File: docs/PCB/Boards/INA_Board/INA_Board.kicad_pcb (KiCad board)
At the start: 2 copper layers, 64.2 x 35.6 mm, 24 parts, among them J1 COM, J2 INA, Q1 AO3407A, SW1 SW_DIP_x02, U1 INA226AIDGST, U2 SIP32431DR3-T1GE3

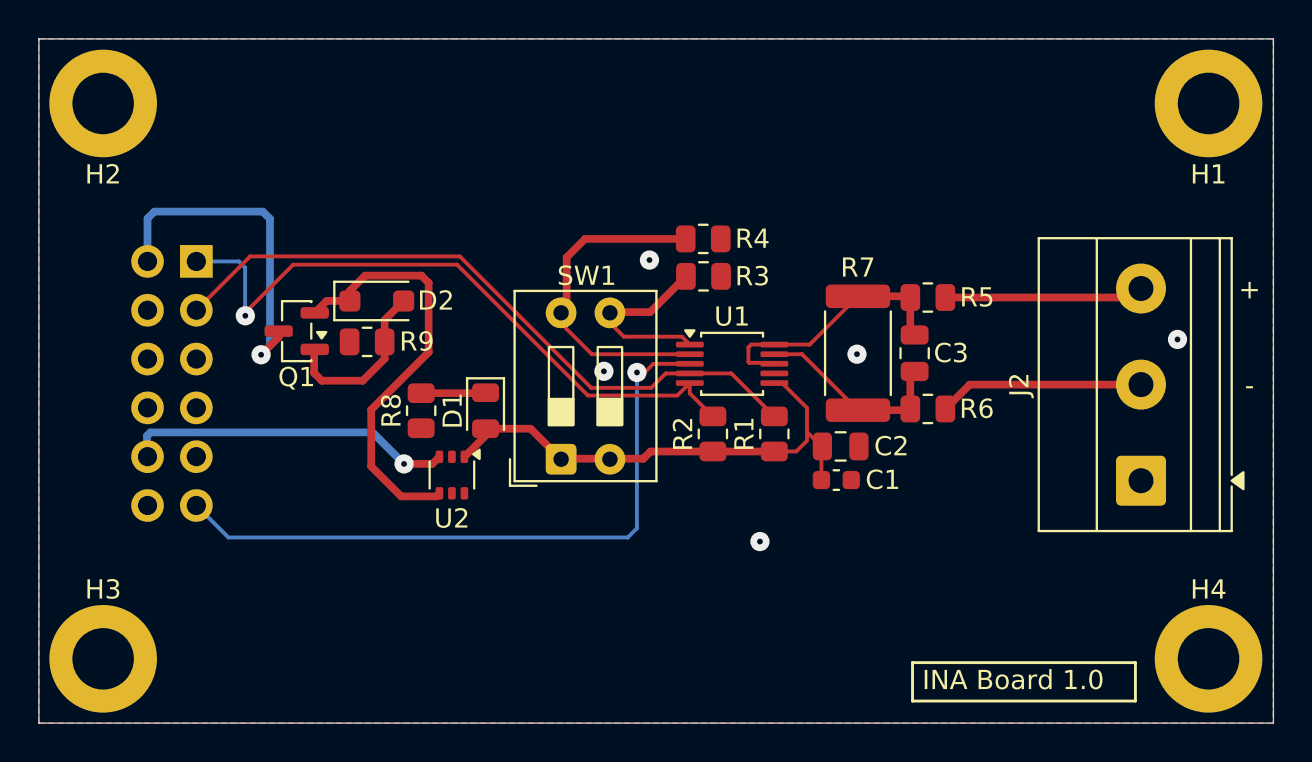
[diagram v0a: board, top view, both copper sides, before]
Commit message: Test program added, can protocol added.
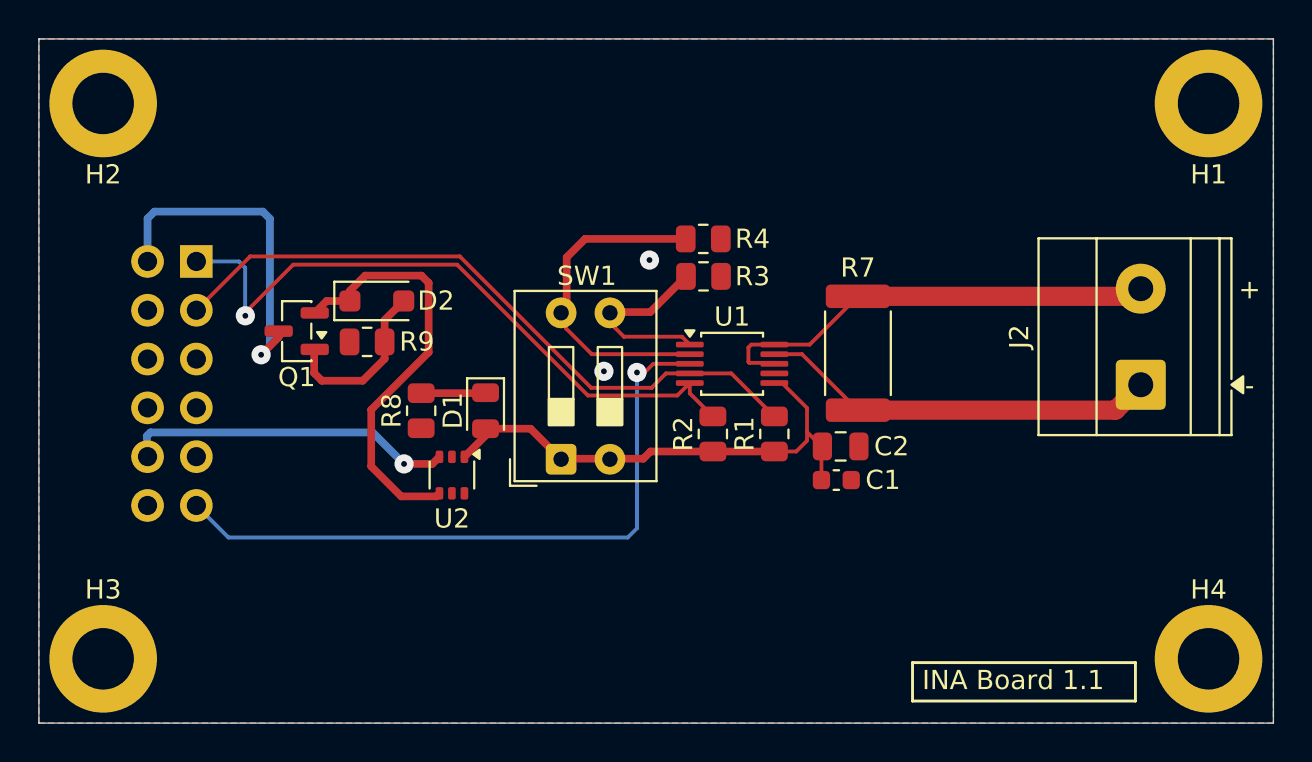
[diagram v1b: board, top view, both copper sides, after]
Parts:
- removed C3: 100nF, Capacitor_SMD:C_0805_2012Metric
- removed R5, R6: 10, Resistor_SMD:R_0805_2012Metric
- J2: footprint TerminalBlock_Phoenix:TerminalBlock_Phoenix_MKDS-1,5-3_1x03_P5.00mm_Horizontal -> TerminalBlock_Phoenix:TerminalBlock_Phoenix_MKDS-1,5-2_1x02_P5.00mm_Horizontal
- moved J2 4.99 mm to (172.9, 83.7)
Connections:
- J2 pad 1: GND -> INA-
- J2 pad 2: INA- -> INA+
- R7 pad 1: Net-(U1-Vbus) -> INA+
- R7 pad 2: Net-(U1-Vin-) -> INA-
- U1 pad 10: Net-(U1-Vbus) -> INA+
- U1 pad 8: Net-(U1-Vbus) -> INA+
- U1 pad 9: Net-(U1-Vin-) -> INA-
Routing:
- net INA+: track 10.4 -> 24.4 mm
- net Net-(U1-Vbus): track 13.5 -> 0.00 mm
- net Net-(U1-Vin-): track 10.4 -> 0.00 mm
- net INA-: track 10.7 -> 20.9 mm
- net GND: vias 5 -> 2
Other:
- board text added: "INA Board 1.1"
- board text removed: "INA Board 1.0"

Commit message: Boards modified.
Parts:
- added C3: 100nF, Capacitor_SMD:C_0805_2012Metric, F.Cu at (157.5, 81.5)
- added C4: 100nF, Capacitor_SMD:C_0805_2012Metric, F.Cu at (155.6, 73.8)
- added R10: 10R, Resistor_SMD:R_0805_2012Metric, F.Cu at (155.6, 75.8)
- added R5: 10R, Resistor_SMD:R_0805_2012Metric, F.Cu at (160.5, 78.7)
- added R6: 10R, Resistor_SMD:R_0805_2012Metric, F.Cu at (160.6, 84.7)
- moved R7 6.64 mm to (164.8, 81.5)
- moved U1 0.99 mm to (152.7, 82.6)
- moved C1 0.69 mm to (157.1, 89.3)
- moved C2 0.69 mm to (157.3, 87.6)
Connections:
- U1 pad 10: INA+ -> Net-(U1-Vin+)
- U1 pad 8: INA+ -> Net-(U1-Vbus)
- U1 pad 9: INA- -> Net-(U1-Vin-)
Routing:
- net Net-(U1-Vin+): track 0.00 -> 13.0 mm
- net Net-(U1-Vbus): track 0.00 -> 12.5 mm
- net INA+: track 24.4 -> 12.7 mm
- net INA-: track 20.9 -> 13.4 mm
- net Net-(U1-Vin-): track 0.00 -> 6.20 mm
- net I2C0_SCL: track 34.8 -> 36.3 mm
- net Net-(U1-A0): track 17.3 -> 18.3 mm
- net Alert: track 34.9 -> 35.9 mm
- net Net-(U1-A1): track 9.65 -> 10.6 mm

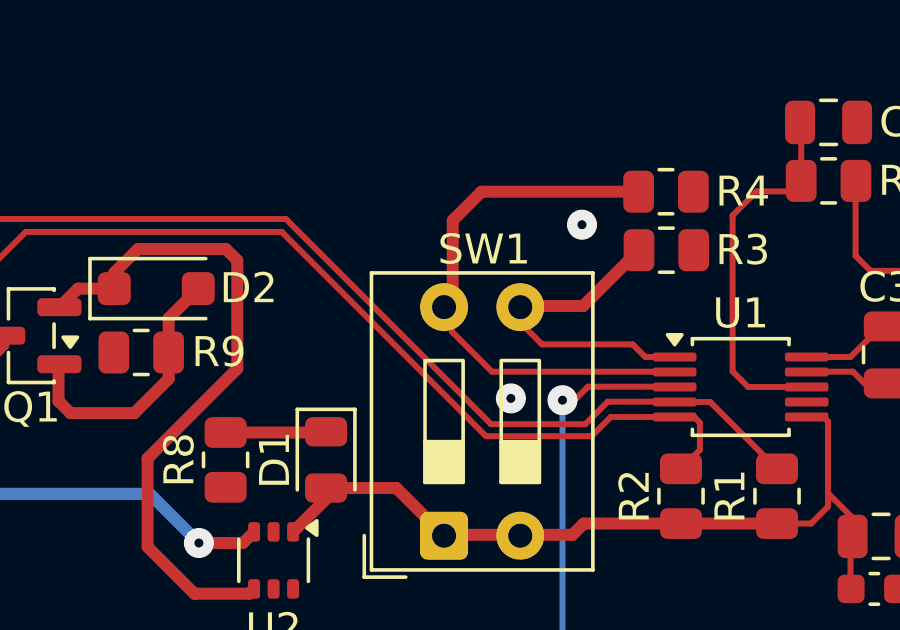
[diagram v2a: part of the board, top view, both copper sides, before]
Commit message: Logger IoT B and C production files generated, backend and frontend prepared for new logger type.
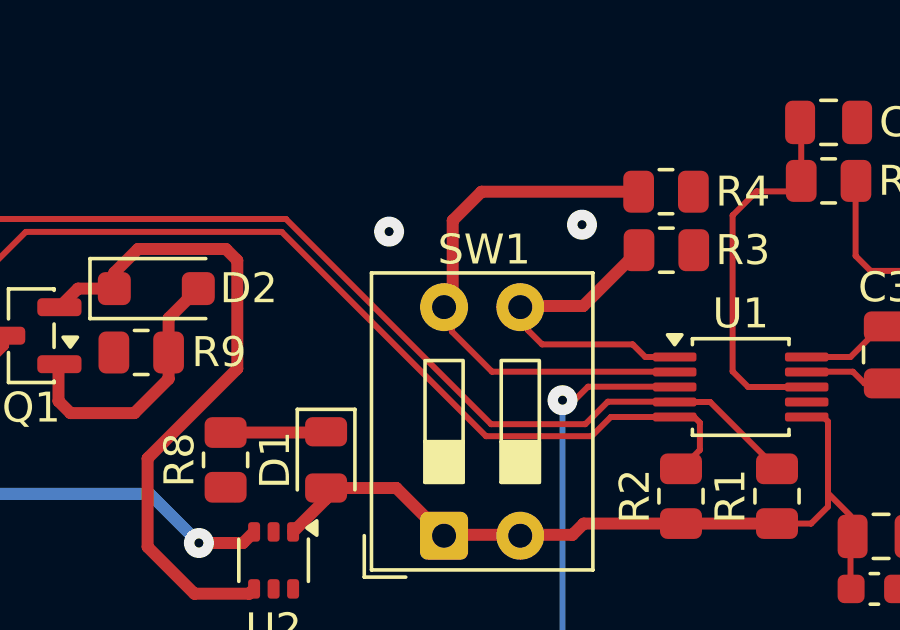
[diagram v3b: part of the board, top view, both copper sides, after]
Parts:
- R8: value 1K -> 4k7R
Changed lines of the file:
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@@
 			)
 		)
-		(property "Value" "1K"
+		(property "Value" "4k7R"
 			(at 0 1.65 90)
 			(layer "F.Fab")
@@
 	)
 	(via
-		(at 145.01 83)
+		(at 140.95 77.44)
 		(size 1)
 		(drill 0.3)
@@
 	)
 	(segment
-		(start 147.58 82.61)
-		(end 150.46 82.61)
+		(start 150.46 82.61)
+		(end 150.47 82.62)
 		(width 0.2)
 		(layer "F.Cu")
@@
 	)
 	(segment
-		(start 147.13 83.06)
-		(end 147.58 82.61)
+		(start 146.73 83.06)
+		(end 147.13 83.06)
 		(width 0.2)
 		(layer "F.Cu")
@@
 	)
 	(segment
-		(start 150.46 82.61)
-		(end 150.47 82.62)
+		(start 147.13 83.06)
+		(end 147.58 82.61)
 		(width 0.2)
 		(layer "F.Cu")
@@
 	)
 	(segment
-		(start 146.73 83.06)
-		(end 147.13 83.06)
+		(start 147.58 82.61)
+		(end 150.46 82.61)
 		(width 0.2)
 		(layer "F.Cu")
@@
 	)
 	(segment
-		(start 125.465 91.6475)
-		(end 123.8 89.9825)
+		(start 146.2525 91.6475)
+		(end 125.465 91.6475)
 		(width 0.2)
 		(layer "B.Cu")
@@
 	)
 	(segment
-		(start 146.2525 91.6475)
-		(end 125.465 91.6475)
+		(start 125.465 91.6475)
+		(end 123.8 89.9825)
 		(width 0.2)
 		(layer "B.Cu")
